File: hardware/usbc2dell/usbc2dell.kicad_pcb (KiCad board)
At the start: 2 copper layers, 39.5 x 26.5 mm, 20 parts, among them J1 USB_C_Receptacle_PowerOnly_6P, J2 DELL_Charger, Q1 Q_NMOS_GDS, Q2 Q_NPN_BEC, SW1 SW_DIP_x04, U1 ATtiny1616-M, U2 FUSB302BMPX, U3 L7805

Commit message: slightly miserable trace routing
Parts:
- moved D2 0.60 mm to (108.2, 81.5)
- moved D1 0.10 mm to (119.6, 80.5)
- turned U1 to 180 degrees
- turned U2 to 0 degrees
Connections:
- U1 pad 6: /LED_R -> /LED_G
- U1 pad 7: /LED_G -> /LED_R
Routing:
- net VCC: track 0.00 -> 34.9 mm, vias 0 -> 2
- net /CC1: track 0.00 -> 32.5 mm, vias 0 -> 3
- net /CC2: track 0.00 -> 26.0 mm, vias 0 -> 2
- net /S0: track 0.00 -> 23.4 mm, vias 0 -> 1
- net /S1: track 0.00 -> 22.1 mm, vias 0 -> 1
- net /S2: track 0.00 -> 20.8 mm, vias 0 -> 1
- net /S3: track 0.00 -> 20.5 mm, vias 0 -> 1
- net Net-(U1-~{RESET}/PA0): track 0.00 -> 17.0 mm, vias 0 -> 1
- net Net-(JP1-A): track 0.00 -> 16.1 mm, vias 0 -> 2
- net /ID_PIN: track 0.00 -> 14.4 mm
- net GND: track 0.00 -> 14.1 mm, vias 44 -> 45
- net Net-(U1-PA1): track 0.00 -> 13.2 mm, vias 0 -> 1
- net /FUSB_INT: track 0.00 -> 13.0 mm, vias 0 -> 2
- net /PWR_EN: track 0.00 -> 11.6 mm, vias 0 -> 2
- net Net-(U1-PA2): track 0.00 -> 11.5 mm, vias 0 -> 1
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- added copper zone on B.Cu, net VBUS
- added copper zone on F.Cu, net VBUS

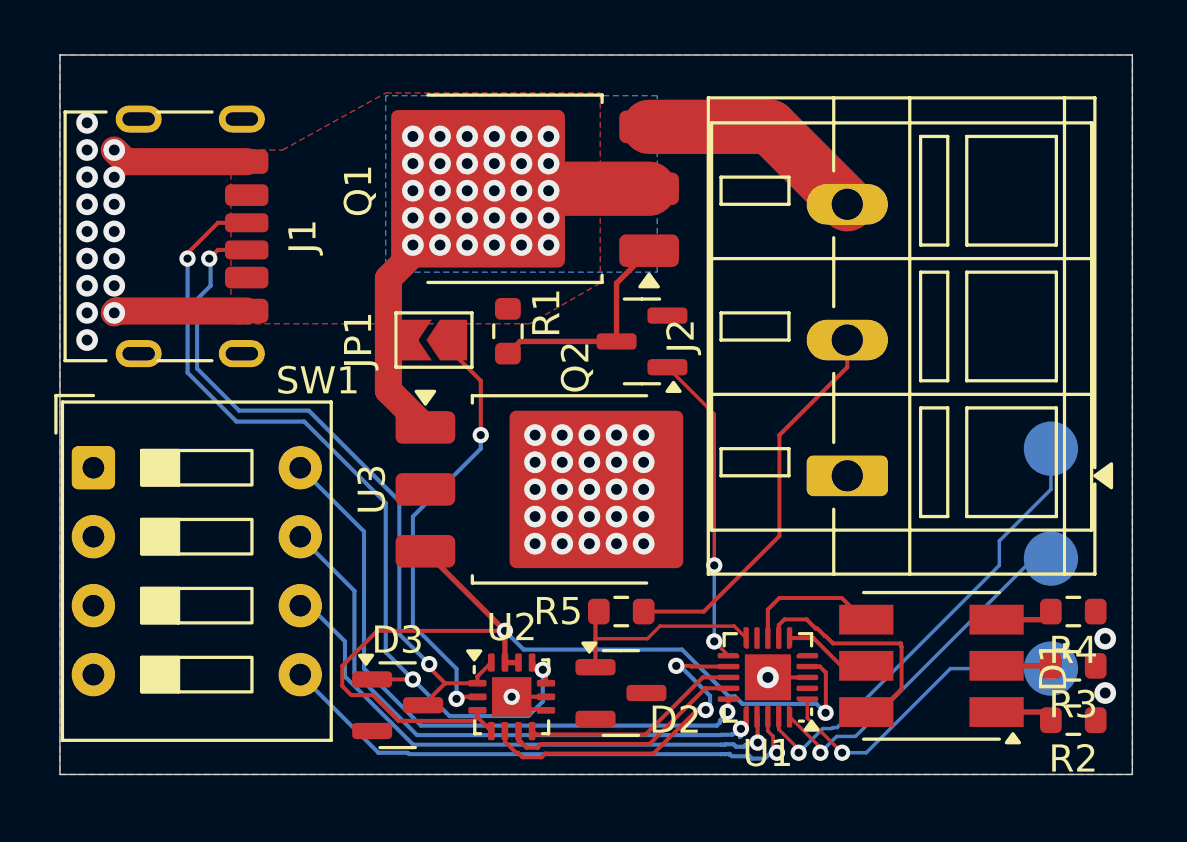
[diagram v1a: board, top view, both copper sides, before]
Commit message: add ziptie-holes
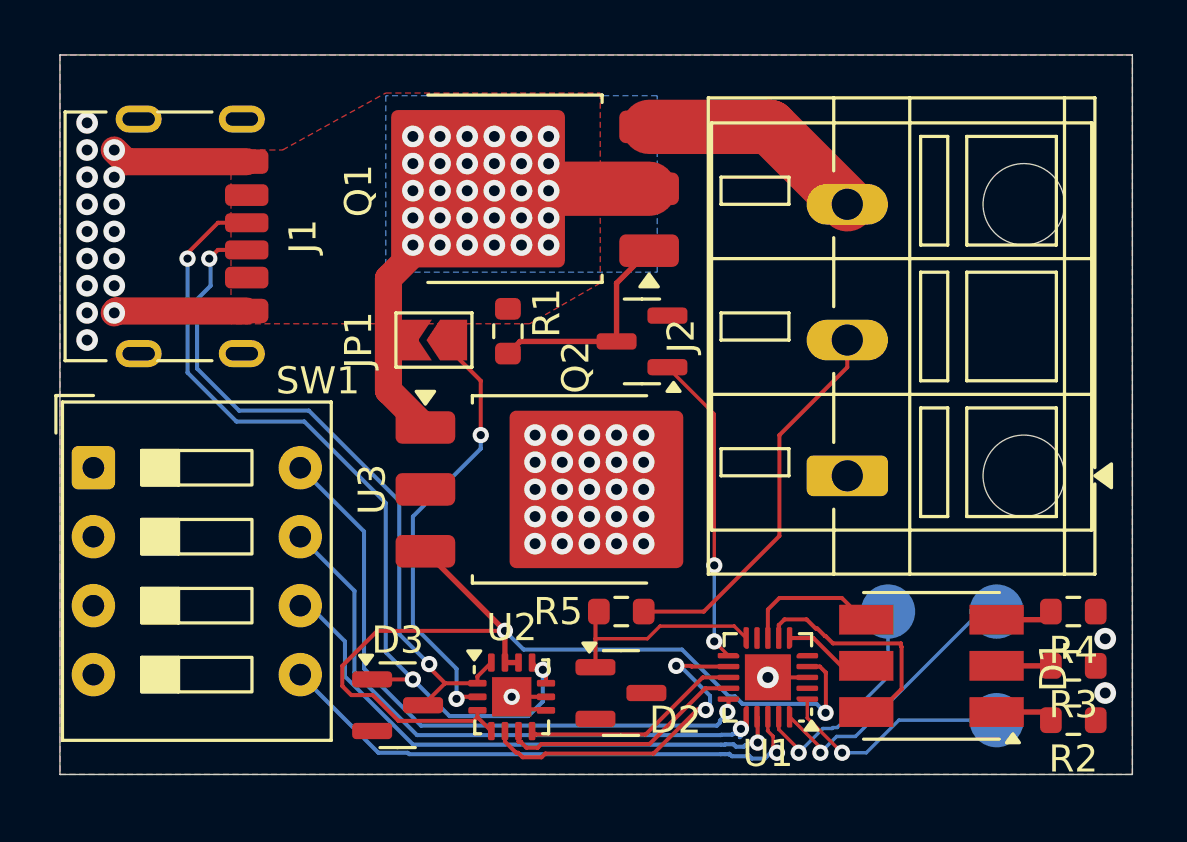
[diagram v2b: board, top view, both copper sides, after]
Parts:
- added REF**: MountingHole_3mm, MountingHole:MountingHole_3mm, F.Cu at (123.0, 73.5)
- added REF**: MountingHole_3mm, MountingHole:MountingHole_3mm, F.Cu at (123.0, 63.5)
- moved TP1 8.49 mm to (118.0, 78.5)
- moved TP2 2.79 mm to (122.0, 78.5)
- moved TP3 2.76 mm to (122.0, 82.5)
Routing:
- net Net-(U1-~{RESET}/PA0): track 17.0 -> 8.48 mm
- net Net-(U1-PA2): track 11.5 -> 8.79 mm
- net Net-(U1-PA1): track 13.2 -> 10.6 mm
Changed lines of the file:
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@@
 		(embedded_fonts no)
 	)
+	(footprint "MountingHole:MountingHole_3mm"
+		(layer "F.Cu")
+		(at 123 73.5)
+		(descr "Mounting Hole 3mm, no annular")
+		(tags "mounting hole 3mm no annular")
+		(property "Reference" "REF**"
+			(at 0 -4 0)
+			(layer "F.SilkS")
+			(hide yes)
+			(effects
+				(font
+					(size 1 1)
+					(thickness 0.15)
+				)
+			)
+		)
+		(property "Value" "MountingHole_3mm"
+			(at 0 4 0)
+			(layer "F.Fab")
+			(effects
+				(font
+					(size 1 1)
+					(thickness 0.15)
+				)
+			)
+		)
+		(property "Datasheet" ""
+			(at 0 0 0)
+			(unlocked yes)
+			(layer "F.Fab")
+			(hide yes)
+			(effects
+				(font
+					(size 1.27 1.27)
+					(thickness 0.15)
+				)
+			)
+		)
+		(property "Description" ""
+			(at 0 0 0)
+			(unlocked yes)
+			(layer "F.Fab")
+			(hide yes)
+			(effects
+				(font
+					(size 1.27 1.27)
+					(thickness 0.15)
+				)
+			)
+		)
+		(attr board_only exclude_from_pos_files exclude_from_bom)
+		(fp_circle
+			(center 0 0)
+			(end 3 0)
+			(stroke
+				(width 0.15)
+				(type solid)
+			)
+			(fill no)
+			(layer "Cmts.User")
+		)
+		(fp_circle
+			(center 0 0)
+			(end 3.25 0)
+			(stroke
+				(width 0.05)
+				(type solid)
+			)
+			(fill no)
+			(layer "F.CrtYd")
+		)
+		(fp_text user "${REFERENCE}"
+			(at 0 0 0)
+			(layer "F.Fab")
+			(effects
+				(font
+					(size 1 1)
+					(thickness 0.15)
+				)
+			)
+		)
+		(pad "" np_thru_hole circle
+			(at 0 0)
+			(size 3 3)
+			(drill 3)
+			(layers "*.Cu" "*.Mask")
+		)
+		(embedded_fonts no)
+	)
 	(footprint "Resistor_SMD:R_0603_1608Metric"
 		(layer "F.Cu")
@@
 		)
 	)
+	(footprint "MountingHole:MountingHole_3mm"
+		(layer "F.Cu")
+		(at 123 63.5)
+		(descr "Mounting Hole 3mm, no annular")
+		(tags "mounting hole 3mm no annular")
+		(property "Reference" "REF**"
+			(at 0 -4 0)
+			(layer "F.SilkS")
+			(hide yes)
+			(effects
+				(font
+					(size 1 1)
+					(thickness 0.15)
+				)
+			)
+		)
+		(property "Value" "MountingHole_3mm"
+			(at 0 4 0)
+			(layer "F.Fab")
+			(effects
+				(font
+					(size 1 1)
+					(thickness 0.15)
+				)
+			)
+		)
+		(property "Datasheet" ""
+			(at 0 0 0)
+			(unlocked yes)
+			(layer "F.Fab")
+			(hide yes)
+			(effects
+				(font
+					(size 1.27 1.27)
+					(thickness 0.15)
+				)
+			)
+		)
+		(property "Description" ""
+			(at 0 0 0)
+			(unlocked yes)
+			(layer "F.Fab")
+			(hide yes)
+			(effects
+				(font
+					(size 1.27 1.27)
+					(thickness 0.15)
+				)
+			)
+		)
+		(attr board_only exclude_from_pos_files exclude_from_bom)
+		(fp_circle
+			(center 0 0)
+			(end 3 0)
+			(stroke
+				(width 0.15)
+				(type solid)
+			)
+			(fill no)
+			(layer "Cmts.User")
+		)
+		(fp_circle
+			(center 0 0)
+			(end 3.25 0)
+			(stroke
+				(width 0.05)
+				(type solid)
+			)
+			(fill no)
+			(layer "F.CrtYd")
+		)
+		(fp_text user "${REFERENCE}"
+			(at 0 0 0)
+			(layer "F.Fab")
+			(effects
+				(font
+					(size 1 1)
+					(thickness 0.15)
+				)
+			)
+		)
+		(pad "" np_thru_hole circle
+			(at 0 0)
+			(size 3 3)
+			(drill 3)
+			(layers "*.Cu" "*.Mask")
+		)
+		(embedded_fonts no)
+	)
 	(footprint "Button_Switch_THT:SW_DIP_SPSTx04_Slide_9.78x12.34mm_W7.62mm_P2.54mm"
 		(layer "F.Cu")
@@
 	(footprint "TestPoint:TestPoint_Pad_D2.0mm"
 		(layer "B.Cu")
-		(at 124 72.5 180)
+		(at 118 78.5 180)
 		(descr "SMD pad as test Point, diameter 2.0mm")
 		(tags "test point SMD pad")
@@
 	(footprint "TestPoint:TestPoint_Pad_D2.0mm"
 		(layer "B.Cu")
-		(at 124 80.6 180)
+		(at 122 82.5 180)
 		(descr "SMD pad as test Point, diameter 2.0mm")
 		(tags "test point SMD pad")
@@
 	(footprint "TestPoint:TestPoint_Pad_D2.0mm"
 		(layer "B.Cu")
-		(at 124 76.55 180)
+		(at 122 78.5 180)
 		(descr "SMD pad as test Point, diameter 2.0mm")
 		(tags "test point SMD pad")
@@
 	)
 	(segment
-		(start 122.1 75.9)
-		(end 124 74)
-		(width 0.127)
-		(layer "B.Cu")
-		(net 22)
-	)
-	(segment
-		(start 116.128 82.772)
-		(end 122.1 76.8)
+		(start 118 80.9)
+		(end 116.128 82.772)
 		(width 0.127)
 		(layer "B.Cu")
@@
 	)
 	(segment
-		(start 124 74)
-		(end 124 72.5)
-		(width 0.127)
-		(layer "B.Cu")
-		(net 22)
-	)
-	(segment
 		(start 115.973211 82.772)
 		(end 116.128 82.772)
@@
 	)
 	(segment
-		(start 122.1 76.8)
-		(end 122.1 75.9)
+		(start 114.70907 83.7)
+		(end 115.60157 82.8075)
 		(width 0.127)
 		(layer "B.Cu")
@@
 	)
 	(segment
-		(start 114.70907 83.7)
-		(end 115.60157 82.8075)
+		(start 118 78.5)
+		(end 118 80.9)
 		(width 0.127)
 		(layer "B.Cu")
@@
 	)
 	(segment
-		(start 116.109073 83.1)
-		(end 116.8 83.1)
+		(start 121.45 78.45)
+		(end 122.1 78.45)
 		(width 0.127)
 		(layer "B.Cu")
@@
 	)
 	(segment
-		(start 123.35 76.55)
-		(end 124 76.55)
+		(start 115.509073 83.7)
+		(end 116.109073 83.1)
 		(width 0.127)
 		(layer "B.Cu")
@@
 	)
 	(segment
-		(start 115.509073 83.7)
-		(end 116.109073 83.1)
+		(start 116.8 83.1)
+		(end 121.45 78.45)
 		(width 0.127)
 		(layer "B.Cu")
@@
 	)
 	(segment
-		(start 116.8 83.1)
-		(end 123.35 76.55)
+		(start 116.109073 83.1)
+		(end 116.8 83.1)
 		(width 0.127)
 		(layer "B.Cu")
@@
 	)
 	(segment
-		(start 120.3 80.6)
-		(end 124 80.6)
+		(start 122 82.5)
+		(end 122.1 82.5)
 		(width 0.127)
 		(layer "B.Cu")
@@
 	)
 	(segment
+		(start 118.4 82.5)
+		(end 122 82.5)
+		(width 0.127)
+		(layer "B.Cu")
+		(net 24)
+	)
+	(segment
 		(start 117.2 83.7)
-		(end 120.3 80.6)
+		(end 118.4 82.5)
 		(width 0.127)
 		(layer "B.Cu")
